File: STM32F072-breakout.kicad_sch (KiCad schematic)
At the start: 31 parts, among them J1 USB_B_Micro, J2 Conn_01x04_Pin, J3 Conn_01x30_Pin, J4 Conn_01x30_Pin, SW1 SW_SPST, U1 STM32F072RBTx, U2 XC6206P332MR, Y1 8MHz

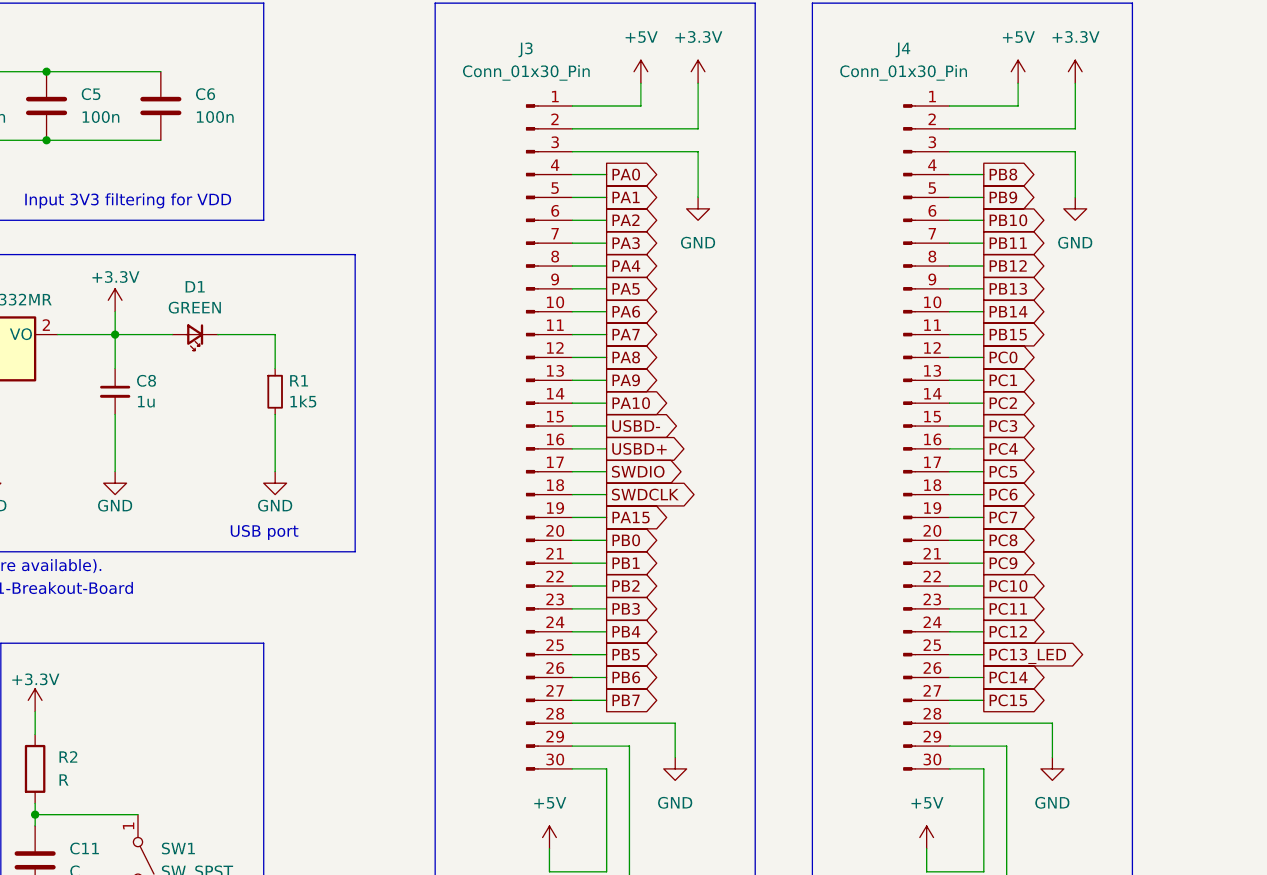
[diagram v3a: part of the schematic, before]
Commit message: reroute headers
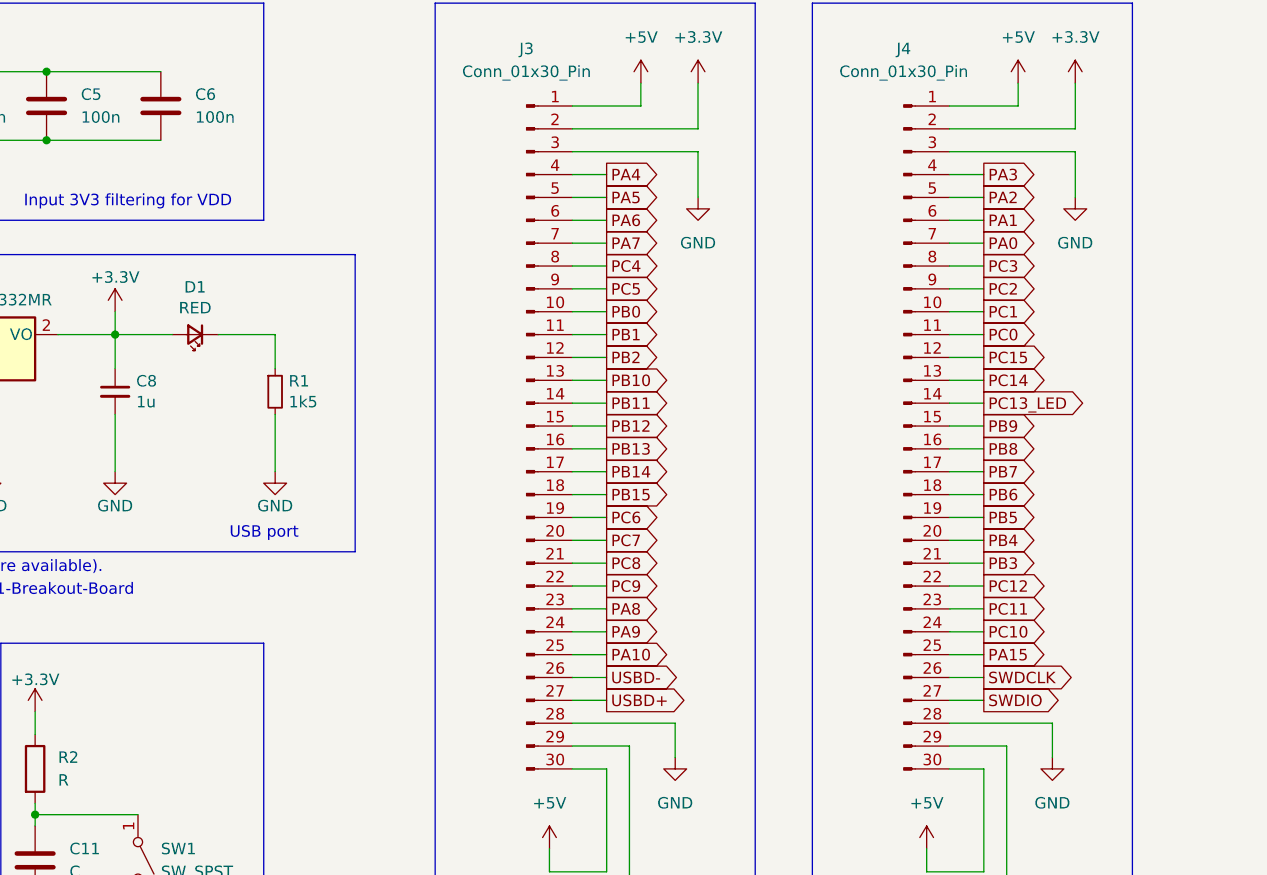
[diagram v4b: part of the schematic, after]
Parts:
- C11, C14: footprint (none) -> Capacitor_SMD:C_0603_1608Metric
- C13: footprint Capacitor_SMD:C_0805_2012Metric -> Capacitor_SMD:C_0603_1608Metric
- D1: value GREEN -> RED
- JP1: footprint (none) -> Jumper:SolderJumper-2_P1.3mm_Open_Pad1.0x1.5mm
- R3, R4: footprint (none) -> Resistor_SMD:R_0603_1608Metric
- SW1: footprint (none) -> Button_Switch_SMD:SW_SPST_EVQPE1
- Y1: footprint (none) -> Crystal:Crystal_SMD_0603-2Pin_6.0x3.5mm
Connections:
- net PA0: now also J4.7 (Pin_7); no longer J3.4 (Pin_4)
- net PA1: now also J4.6 (Pin_6); no longer J3.5 (Pin_5)
- net PA10: now also J3.25 (Pin_25); no longer J3.14 (Pin_14)
- net PA15: now also J4.25 (Pin_25); no longer J3.19 (Pin_19)
- net PA2: now also J4.5 (Pin_5); no longer J3.6 (Pin_6)
- net PA3: now also J4.4 (Pin_4); no longer J3.7 (Pin_7)
- net PA4: now also J3.4 (Pin_4); no longer J3.8 (Pin_8)
- net PA5: now also J3.5 (Pin_5); no longer J3.9 (Pin_9)
- net PA6: now also J3.6 (Pin_6); no longer J3.10 (Pin_10)
- net PA7: now also J3.7 (Pin_7); no longer J3.11 (Pin_11)
- net PA8: now also J3.23 (Pin_23); no longer J3.12 (Pin_12)
- net PA9: now also J3.24 (Pin_24); no longer J3.13 (Pin_13)
- net PB0: now also J3.10 (Pin_10); no longer J3.20 (Pin_20)
- net PB1: now also J3.11 (Pin_11); no longer J3.21 (Pin_21)
- net PB10: now also J3.13 (Pin_13); no longer J4.6 (Pin_6)
- net PB11: now also J3.14 (Pin_14); no longer J4.7 (Pin_7)
- net PB12: now also J3.15 (Pin_15); no longer J4.8 (Pin_8)
- net PB13: now also J3.16 (Pin_16); no longer J4.9 (Pin_9)
- net PB14: now also J3.17 (Pin_17); no longer J4.10 (Pin_10)
- net PB15: now also J3.18 (Pin_18); no longer J4.11 (Pin_11)
- net PB2: now also J3.12 (Pin_12); no longer J3.22 (Pin_22)
- net PB3: now also J4.21 (Pin_21); no longer J3.23 (Pin_23)
- net PB4: now also J4.20 (Pin_20); no longer J3.24 (Pin_24)
- net PB5: now also J4.19 (Pin_19); no longer J3.25 (Pin_25)
- net PB6: now also J4.18 (Pin_18); no longer J3.26 (Pin_26)
- net PB7: now also J4.17 (Pin_17); no longer J3.27 (Pin_27)
- net PB8: now also J4.16 (Pin_16); no longer J4.4 (Pin_4)
- net PB9: now also J4.15 (Pin_15); no longer J4.5 (Pin_5)
- net PC0: now also J4.11 (Pin_11); no longer J4.12 (Pin_12)
- net PC1: now also J4.10 (Pin_10); no longer J4.13 (Pin_13)
- net PC10: now also J4.24 (Pin_24); no longer J4.22 (Pin_22)
- net PC12: now also J4.22 (Pin_22); no longer J4.24 (Pin_24)
- net PC13_LED: now also J4.14 (Pin_14); no longer J4.25 (Pin_25)
- net PC14: now also J4.13 (Pin_13); no longer J4.26 (Pin_26)
- net PC15: now also J4.12 (Pin_12); no longer J4.27 (Pin_27)
- net PC2: now also J4.9 (Pin_9); no longer J4.14 (Pin_14)
- net PC3: now also J4.8 (Pin_8); no longer J4.15 (Pin_15)
- net PC4: now also J3.8 (Pin_8); no longer J4.16 (Pin_16)
- net PC5: now also J3.9 (Pin_9); no longer J4.17 (Pin_17)
- net PC6: now also J3.19 (Pin_19); no longer J4.18 (Pin_18)
- net PC7: now also J3.20 (Pin_20); no longer J4.19 (Pin_19)
- net PC8: now also J3.21 (Pin_21); no longer J4.20 (Pin_20)
- net PC9: now also J3.22 (Pin_22); no longer J4.21 (Pin_21)
- net SWDCLK: now also J4.26 (Pin_26); no longer J3.18 (Pin_18)
- net SWDIO: now also J4.27 (Pin_27); no longer J3.17 (Pin_17)
- net USBD+: now also J3.27 (Pin_27); no longer J3.16 (Pin_16)
- net USBD-: now also J3.26 (Pin_26); no longer J3.15 (Pin_15)

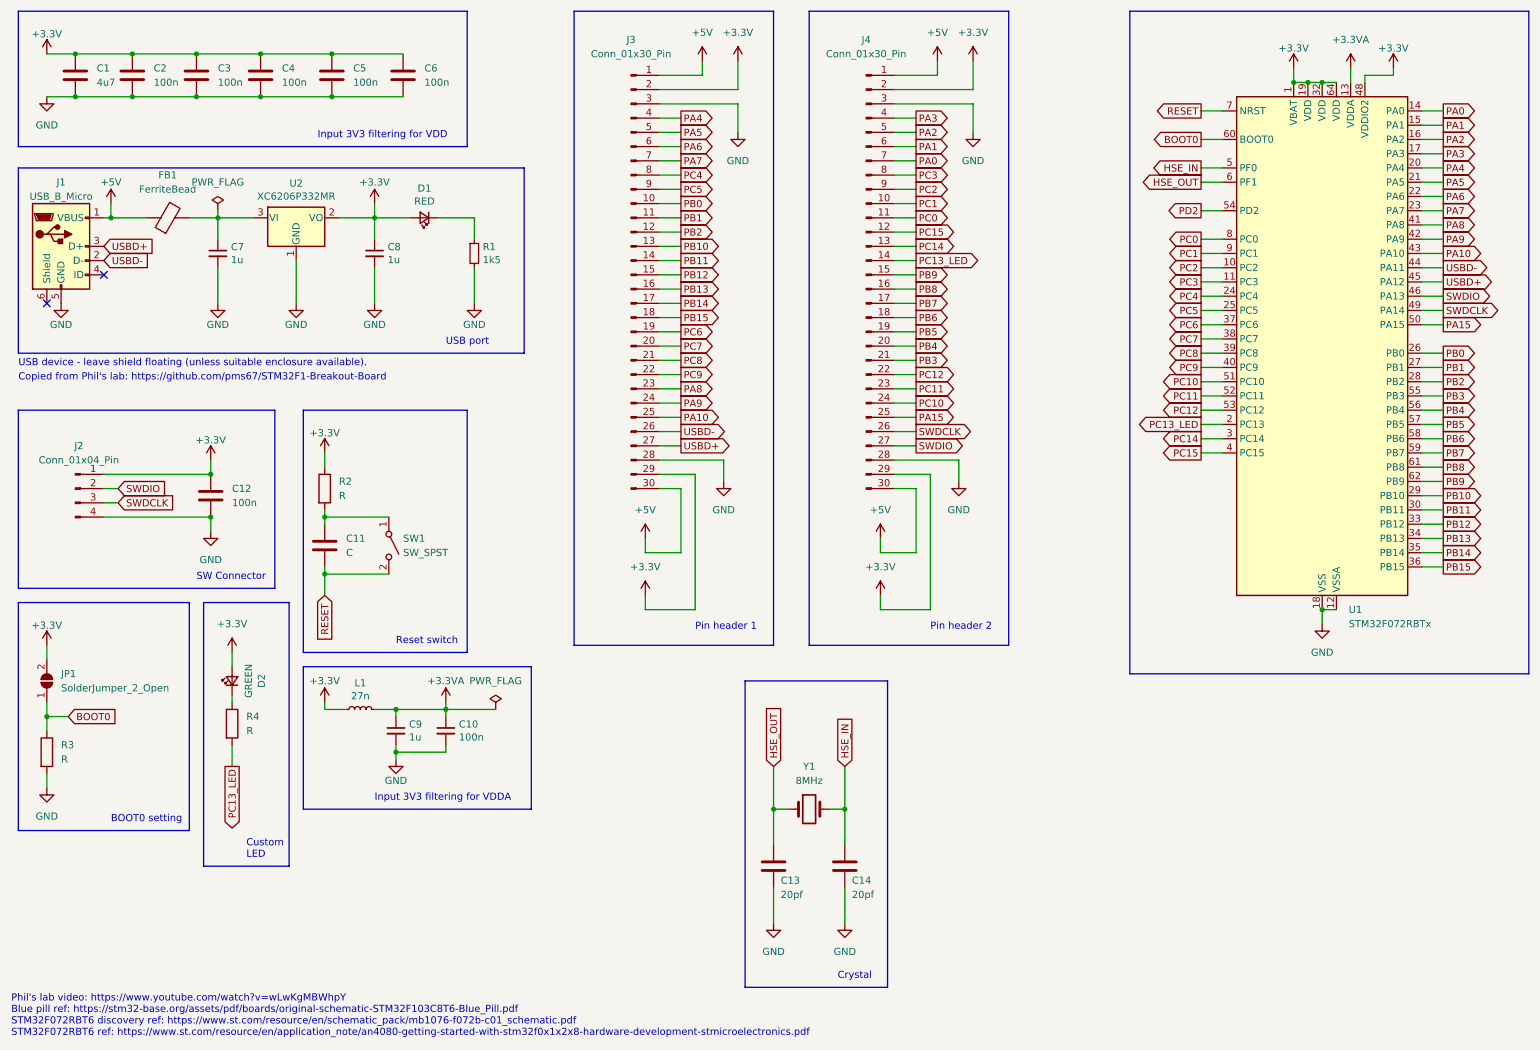
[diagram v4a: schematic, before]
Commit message: add CAN MCP2551
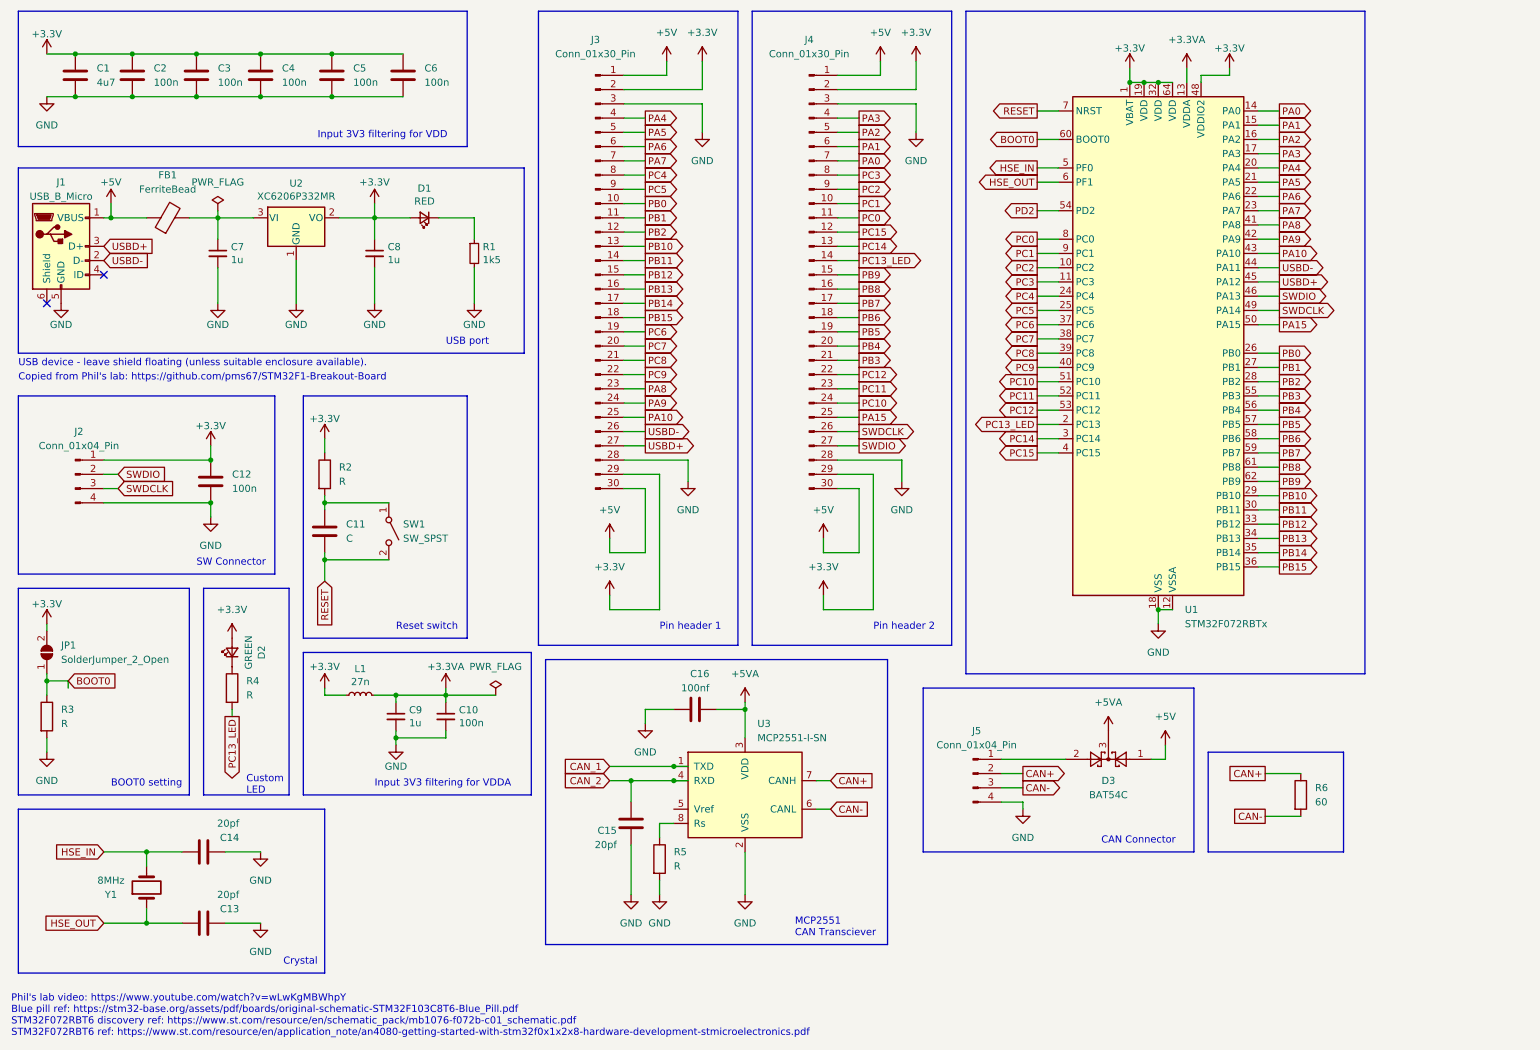
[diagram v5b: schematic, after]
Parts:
- added C15: 20pf, Capacitor_SMD:C_0603_1608Metric, symbol Device:C
- added C16: 100nf, Capacitor_SMD:C_0603_1608Metric, symbol Device:C
- added D3: BAT54C, Package_TO_SOT_SMD:SOT-23, symbol Diode:BAT54C
- added J5: Conn_01x04_Pin, symbol Connector:Conn_01x04_Pin
- added R5: R, Resistor_SMD:R_0805_2012Metric, symbol Device:R
- added R6: 60, Resistor_SMD:R_0805_2012Metric, symbol Device:R
- added U3: MCP2551-I-SN, Package_SO:SOIC-8_3.9x4.9mm_P1.27mm, symbol Interface_CAN_LIN:MCP2551-I-SN
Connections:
- net +5V: now also D3.1
- net GND: now also C15.1, C16.1, J5.4 (Pin_4), R5.2, U3.2 (VSS)
- new net: D3.2, J5.1 (Pin_1)
- new net: R5.1, U3.8 (Rs)
- new net +5VA: C16.2, D3.3, U3.3 (VDD)
- new net CAN+: J5.2 (Pin_2), R6.1, U3.7 (CANH)
- new net CAN-: J5.3 (Pin_3), R6.2, U3.6 (CANL)
- new net CAN_1: U3.1 (TXD)
- new net CAN_2: C15.2, U3.4 (RXD)
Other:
- note added: "CAN Connector"
- note added: "MCP2551 CAN Transciever"
- moved on the sheet: C10, C11, C12, C13, C14, C9, D2, J2, J3, J4, JP1, L1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

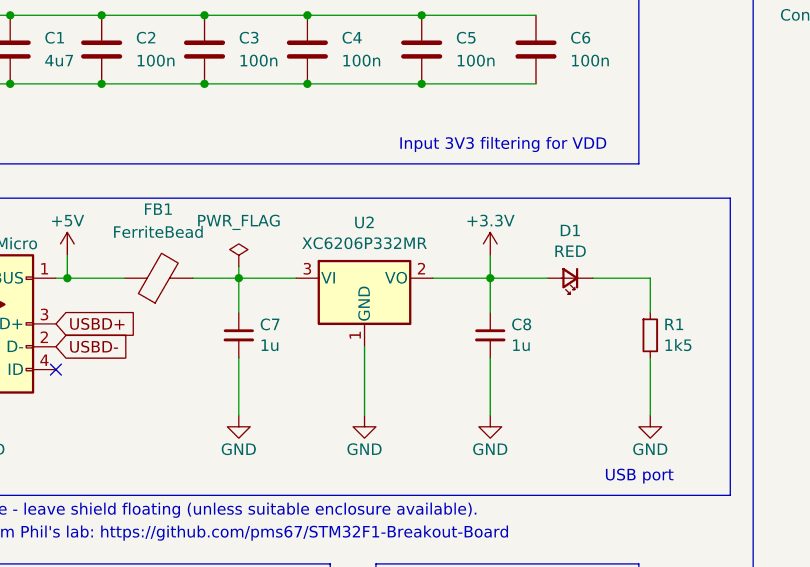
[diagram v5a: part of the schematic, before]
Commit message: use ams1117 for 3.3V
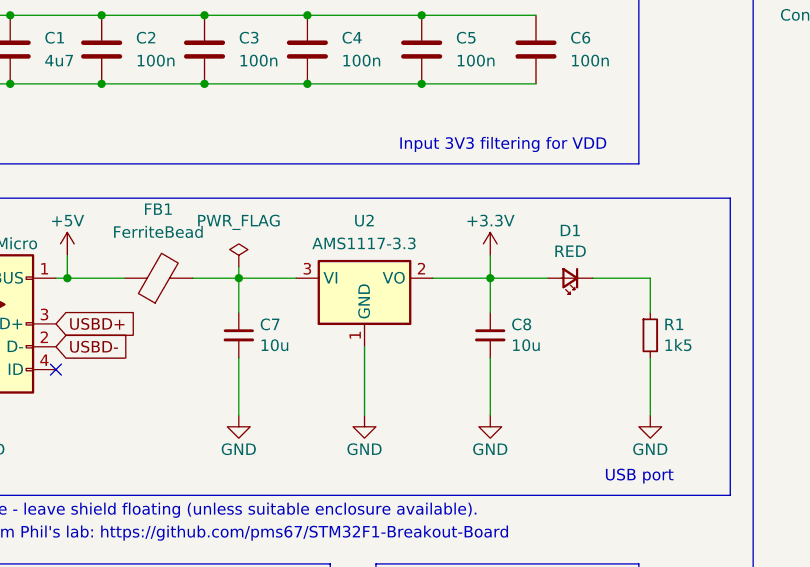
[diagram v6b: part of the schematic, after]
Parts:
- removed U2: XC6206P332MR, Package_TO_SOT_SMD:SOT-23, symbol Regulator_Linear:XC6206PxxxMR
- added U2: AMS1117-3.3, Package_TO_SOT_SMD:SOT-223-3_TabPin2, symbol Regulator_Linear:AMS1117-3.3
- C7, C8: value 1u -> 10u
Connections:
- net +3.3V: now also U2.2 (VO)
- net GND: now also U2.1 (GND)
- net at C7.1, FB1.2: now also U2.3 (VI)
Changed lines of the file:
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@@
       (effects (font (size 1.27 1.27)) (justify left))
     )
-    (property "Value" "1u" (at 51.8668 58.293 0)
+    (property "Value" "10u" (at 51.8668 58.293 0)
       (effects (font (size 1.27 1.27)) (justify left))
     )
@@
         (path "/8c0a2226-64d6-45fd-ae26-77a981e24a27"
           (reference "#PWR011") (unit 1)
-        )
-      )
-    )
-  )
-  (symbol (lib_id "Regulator_Linear:XC6206PxxxMR") (at 63.5 50.8 0) (unit 1)
-    (in_bom yes) (on_board yes) (dnp no)
-    (property "Reference" "U2" (at 63.5 44.6532 0)
-      (effects (font (size 1.27 1.27)))
-    )
-    (property "Value" "XC6206P332MR" (at 63.5 46.9646 0)
-      (effects (font (size 1.27 1.27)))
-    )
-    (property "Footprint" "Package_TO_SOT_SMD:SOT-23" (at 63.5 45.085 0)
-      (effects (font (size 1.27 1.27) italic) hide)
-    )
-    (property "Datasheet" "https://www.torexsemi.com/file/xc6206/XC6206.pdf" (at 63.5 50.8 0)
-      (effects (font (size 1.27 1.27)) hide)
-    )
-    (property "LCSC Part #" "C5446" (at 63.5 50.8 0)
-      (effects (font (size 1.27 1.27)) hide)
-    )
-    (pin "1")
-    (pin "2")
-    (pin "3")
-    (instances
-      (project "STM32F072-breakout"
-        (path "/0d07611c-4323-4af8-b284-ea326e576e1c"
-          (reference "U2") (unit 1)
-        )
-      )
-      (project "SimpleTM32"
-        (path "/8c0a2226-64d6-45fd-ae26-77a981e24a27"
-          (reference "U1") (unit 1)
         )
       )
@@
         (path "/8c0a2226-64d6-45fd-ae26-77a981e24a27"
           (reference "R1") (unit 1)
+        )
+      )
+    )
+  )
+  (symbol (lib_id "Regulator_Linear:AMS1117-3.3") (at 63.5 50.8 0) (unit 1)
+    (in_bom yes) (on_board yes) (dnp no) (fields_autoplaced)
+    (property "Reference" "U2" (at 63.5 44.45 0)
+      (effects (font (size 1.27 1.27)))
+    )
+    (property "Value" "AMS1117-3.3" (at 63.5 46.99 0)
+      (effects (font (size 1.27 1.27)))
+    )
+    (property "Footprint" "Package_TO_SOT_SMD:SOT-223-3_TabPin2" (at 63.5 45.72 0)
+      (effects (font (size 1.27 1.27)) hide)
+    )
+    (property "Datasheet" "http://www.advanced-monolithic.com/pdf/ds1117.pdf" (at 66.04 57.15 0)
+      (effects (font (size 1.27 1.27)) hide)
+    )
+    (pin "1")
+    (pin "2")
+    (pin "3")
+    (instances
+      (project "STM32F072-breakout"
+        (path "/0d07611c-4323-4af8-b284-ea326e576e1c"
+          (reference "U2") (unit 1)
         )
       )
@@
       (effects (font (size 1.27 1.27)) (justify left))
     )
-    (property "Value" "1u" (at 79.8068 58.293 0)
-      (effects (font (size 1.27 1.27)) (justify left))
-    )
+    (property "Value" "10u" (at 79.8068 58.293 0)
+      (effects (font (size 1.27 1.27)) (justify left))
+    )
